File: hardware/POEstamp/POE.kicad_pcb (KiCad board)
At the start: 2 copper layers, 70 x 40 mm, 139 parts, among them J1 0813-1X1T-57-F, P3 GND, P4 +5V, P5 CONN_01X05, P6 5Vout, P7 GNDout, Q1 SI3440DV, NFET, Q2 2N7002, Q3 MMBTA42, T1 PA1134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

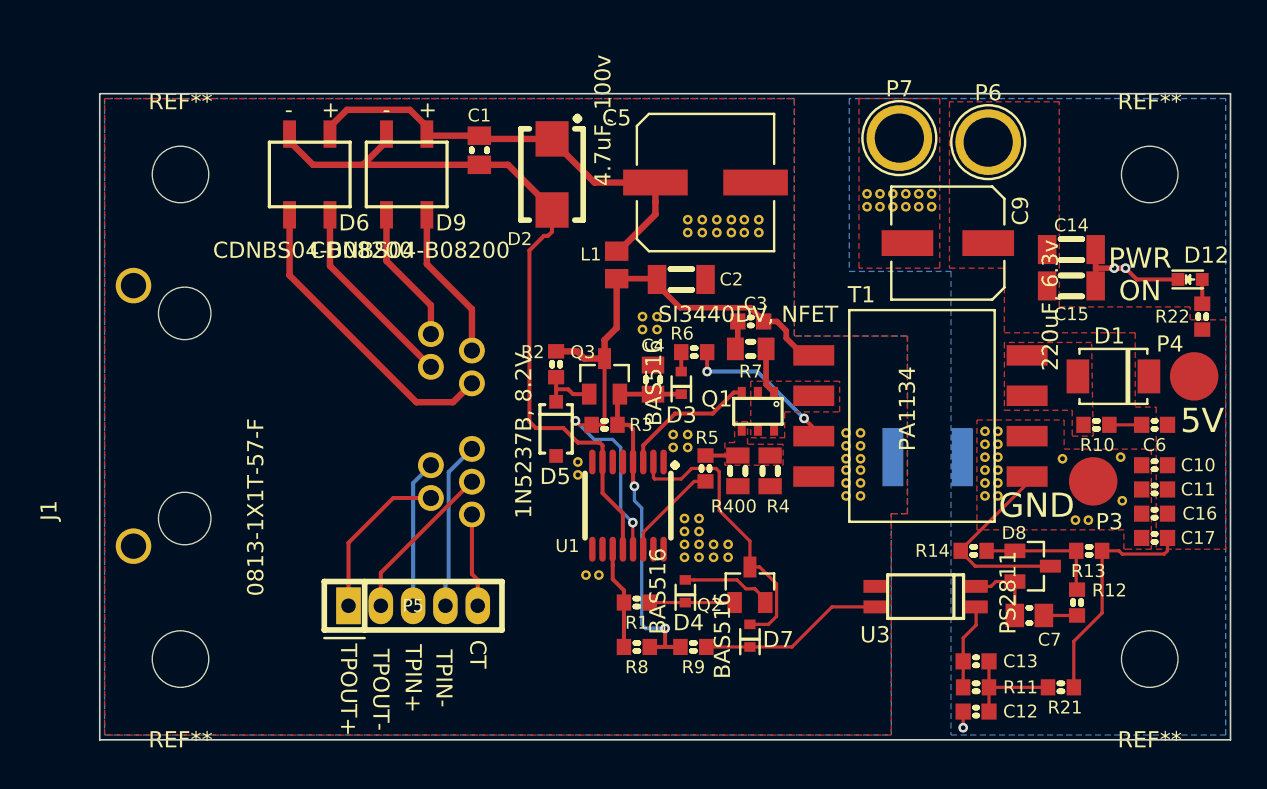
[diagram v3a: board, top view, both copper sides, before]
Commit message: Arranging a few parts on silkscreen a bit differently, also adjusted min size of soldermask to be a bit smaller.
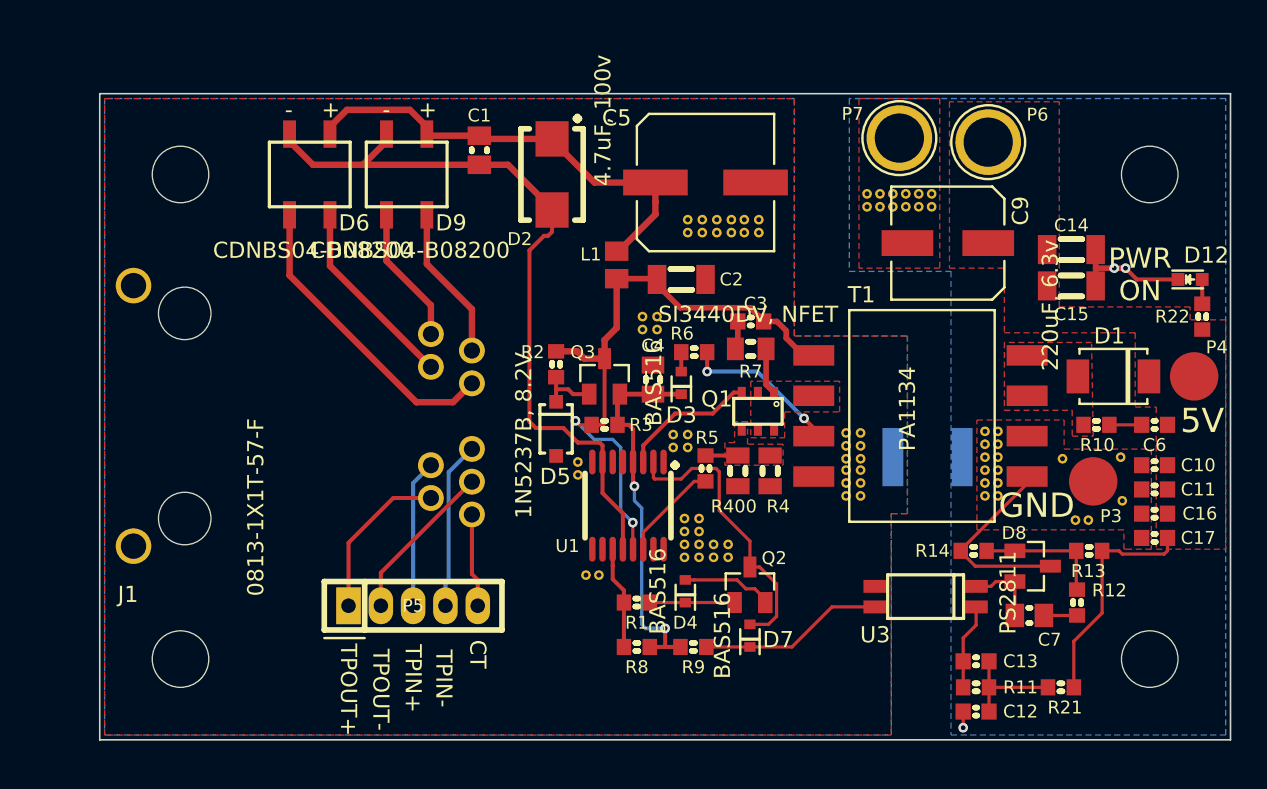
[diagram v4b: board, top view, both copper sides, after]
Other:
- rule pad_to_mask_clearance: 0.07 -> 0.05
- rule solder_mask_min_width: 0.1 -> 0.05
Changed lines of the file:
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@@
     (37 F.SilkS user)
     (38 B.Mask user)
-    (39 F.Mask user hide)
+    (39 F.Mask user)
     (40 Dwgs.User user)
     (41 Cmts.User user)
@@
     (pad_size 0.6 0.6)
     (pad_drill 0.3)
-    (pad_to_mask_clearance 0.07)
-    (solder_mask_min_width 0.1)
+    (pad_to_mask_clearance 0.05)
+    (solder_mask_min_width 0.05)
     (aux_axis_origin 0 0)
     (visible_elements FFFEFF7F)
@@
       (layerselection 0x010f0_80000001)
       (usegerberextensions true)
+      (gerberprecision 5)
       (excludeedgelayer true)
       (linewidth 0.100000)
@@
     (descr "Mounting hole, Befestigungsbohrung, 3,5mm, No Annular, Kein Restring,")
     (tags "Mounting hole, Befestigungsbohrung, 3,5mm, No Annular, Kein Restring,")
-    (fp_text reference REF** (at 0 -4.50088) (layer F.SilkS)
+    (fp_text reference REF** (at 0 -4.50088) (layer F.SilkS) hide
       (effects (font (size 1 1) (thickness 0.15)))
     )
@@
     (descr "Mounting hole, Befestigungsbohrung, 3,5mm, No Annular, Kein Restring,")
     (tags "Mounting hole, Befestigungsbohrung, 3,5mm, No Annular, Kein Restring,")
-    (fp_text reference REF** (at 0 5) (layer F.SilkS)
+    (fp_text reference REF** (at 0 5) (layer F.SilkS) hide
       (effects (font (size 1 1) (thickness 0.15)))
     )
@@
     (descr "Mounting hole, Befestigungsbohrung, 3,5mm, No Annular, Kein Restring,")
     (tags "Mounting hole, Befestigungsbohrung, 3,5mm, No Annular, Kein Restring,")
-    (fp_text reference REF** (at 0 5) (layer F.SilkS)
+    (fp_text reference REF** (at 0 5) (layer F.SilkS) hide
       (effects (font (size 1 1) (thickness 0.15)))
     )
@@
     (descr "Mounting hole, Befestigungsbohrung, 3,5mm, No Annular, Kein Restring,")
     (tags "Mounting hole, Befestigungsbohrung, 3,5mm, No Annular, Kein Restring,")
-    (fp_text reference REF** (at 0 -4.50088) (layer F.SilkS)
+    (fp_text reference REF** (at 0 -4.50088) (layer F.SilkS) hide
       (effects (font (size 1 1) (thickness 0.15)))
     )
@@
     (descr "http://www.diodes.com/datasheets/ap02001.pdf p.144")
     (tags "Diode SOD523")
-    (fp_text reference D4 (at 1.95 -0.2 360) (layer F.SilkS)
-      (effects (font (size 1 1) (thickness 0.15)))
+    (fp_text reference D4 (at 1.95 0 360) (layer F.SilkS)
+      (effects (font (size 0.8 0.8) (thickness 0.15)))
     )
     (fp_text value BAS516 (at 0 1.7 270) (layer F.SilkS)
@@
   (module rfid:0813-1X1T-57-F (layer F.Cu)
     (at 75.26 60.3 90)
-    (fp_text reference J1 (at 0.5 -8.4 90) (layer F.SilkS)
+    (fp_text reference J1 (at -4.7 -3.51 180) (layer F.SilkS)
       (effects (font (size 1 1) (thickness 0.15)))
     )
@@
     (descr "module 1 pin (ou trou mecanique de percage)")
     (tags DEV)
-    (fp_text reference P6 (at 0 -3.048) (layer F.SilkS)
-      (effects (font (size 1 1) (thickness 0.15)))
+    (fp_text reference P6 (at 3.05 -1.7) (layer F.SilkS)
+      (effects (font (size 0.8 0.8) (thickness 0.15)))
     )
     (fp_text value 5Vout (at 0 2.794) (layer F.Fab)
@@
     (descr "module 1 pin (ou trou mecanique de percage)")
     (tags DEV)
-    (fp_text reference P7 (at 0 -3.048) (layer F.SilkS)
-      (effects (font (size 1 1) (thickness 0.15)))
+    (fp_text reference P7 (at -2.9 -1.5) (layer F.SilkS)
+      (effects (font (size 0.8 0.8) (thickness 0.15)))
     )
     (fp_text value GNDout (at 0 2.794) (layer F.Fab)
@@
   (module smd-semi:SOT-23 (layer F.Cu)
     (at 110.25 64.4 90)
-    (fp_text reference Q2 (at -1.25 -2.5 180) (layer F.SilkS)
+    (fp_text reference Q2 (at 1.65 1.5 180) (layer F.SilkS)
       (effects (font (size 0.8 0.8) (thickness 0.15)))
     )
@@
     (descr "Mesurement Point, Round, SMD Pad, DM 3mm,")
     (tags "Mesurement Point, Round, SMD Pad, DM 3mm,")
-    (fp_text reference P3 (at 1 2.5) (layer F.SilkS)
-      (effects (font (size 1 1) (thickness 0.15)))
+    (fp_text reference P3 (at 1.1 2.15) (layer F.SilkS)
+      (effects (font (size 0.8 0.8) (thickness 0.15)))
     )
     (fp_text value GND (at 2.54 3.81) (layer F.Fab)
@@
     (descr "Mesurement Point, Round, SMD Pad, DM 3mm,")
     (tags "Mesurement Point, Round, SMD Pad, DM 3mm,")
-    (fp_text reference P4 (at -1.5 -2) (layer F.SilkS)
-      (effects (font (size 1 1) (thickness 0.15)))
+    (fp_text reference P4 (at 1.4 -1.8) (layer F.SilkS)
+      (effects (font (size 0.8 0.8) (thickness 0.15)))
     )
     (fp_text value +5V (at 2.54 3.81) (layer F.Fab)
